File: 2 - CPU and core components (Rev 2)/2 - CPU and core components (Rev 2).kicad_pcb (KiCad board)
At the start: 2 copper layers, 152.3 x 106.7 mm, 76 parts, among them J1 READ INT MODE, J10 COM 3, J11 COM3 SWAP RX/TX, J2 BUS 1, J3 SIO1 CLK SRC, J4 COM 1, J5 COM 2, J6 SIO2 CLK SRC, J7 COM3 RX 232 BYPASS, J8 COM3 TTL OR 232, J9 DB9 VCC BYPASS, U1 ATF16V8B, U10 AS6C4008, U11 Z84C3010 CTC, U12 Z84C4010, U13 MCP2221A, U14 MCP2221A, U15 Z84C4010, U16 MAX232, U2 ATF22V10C, U3 ATF16V8B, U4 74HCT573, U5 74HCT32, U6 74HCT374, U7 74HCT244, U8 Z84C0010, U9 SST39SF010, X1 10 MHz, X2 3.6864 MHz

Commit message: Replacing a lot of TTL chips by 2 PLDs. Also, added blinkenlights.
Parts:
- removed the C19 at (168.0, 46.7)
- removed C20: 1µF, Capacitor_THT:C_Disc_D3.4mm_W2.1mm_P2.50mm
- removed C21, C22, C23, C24: 1uF, Capacitor_THT:C_Disc_D3.4mm_W2.1mm_P2.50mm
- removed D10, D9: RX3, LED_THT:LED_D3.0mm_Horizontal_O1.27mm_Z2.0mm_Clear
- removed the D7 at (109.3, 95.4)
- removed the D8 at (109.3, 85.3)
- removed J10: COM 3, Connector_Dsub:DSUB-9_Male_Horizontal_P2.77x2.84mm_EdgePinOffset4.94mm_Housed_MountingHolesOffset7.48mm
- removed J11: COM3 SWAP RX/TX, Connector_PinHeader_2.54mm:PinHeader_2x03_P2.54mm_Vertical
- removed J6: SIO2 CLK SRC, Connector_PinHeader_2.54mm:PinHeader_1x03_P2.54mm_Vertical
- removed J7: COM3 RX 232 BYPASS, Connector_PinHeader_2.54mm:PinHeader_1x02_P2.54mm_Vertical
- removed J8: COM3 TTL OR 232, Connector_PinHeader_2.54mm:PinHeader_2x03_P2.54mm_Vertical
- removed J9: DB9 VCC BYPASS, Connector_PinHeader_2.54mm:PinHeader_1x02_P2.54mm_Vertical
- removed R7: 3K3, Resistor_THT:R_Axial_DIN0207_L6.3mm_D2.5mm_P10.16mm_Horizontal
- removed R8: 330, Resistor_THT:R_Axial_DIN0207_L6.3mm_D2.5mm_P10.16mm_Horizontal
- removed R9: 220, Resistor_THT:R_Axial_DIN0207_L6.3mm_D2.5mm_P10.16mm_Horizontal
- removed the U15 at (171.2, 74.8)
- removed the U16 at (225.9, 37.8)
- removed the U3 at (161.2, 125.1)
- removed the U4 at (196.8, 110.9)
- added BAR1: F2010BW, 0_Library:BAR_GRAPH_8, F.Cu at (120.6, 125.2)
- added C10: 1µF, Capacitor_THT:C_Disc_D3.0mm_W2.0mm_P2.50mm, F.Cu at (52.0, 82.4)
- added RN5: 330, Resistor_THT:R_Array_SIP9, F.Cu at (109.2, 126.4)
- added U17: 74HCT240, Package_DIP:DIP-20_W7.62mm_Socket, F.Cu at (73.0, 53.4)
- added U2: 74HCT74, Package_DIP:DIP-14_W7.62mm_Socket, F.Cu at (18.1, 49.1)
- added U5: ATF22V10C, Package_DIP:DIP-24_W7.62mm, F.Cu at (41.2, 68.5)
- added U8: 74HCT32, Package_DIP:DIP-14_W7.62mm_Socket, F.Cu at (29.9, 49.1)
- added U9: 74HCT373, Package_DIP:DIP-20_W7.62mm_Socket, F.Cu at (29.9, 68.6)
- C1, C2, C3, C4, C7: footprint Capacitor_THT:C_Disc_D3.4mm_W2.1mm_P2.50mm -> Capacitor_THT:C_Disc_D3.0mm_W1.6mm_P2.50mm
- C5, C6, C8, C9: footprint Capacitor_THT:C_Disc_D3.4mm_W2.1mm_P2.50mm -> Capacitor_THT:C_Disc_D3.0mm_W2.0mm_P2.50mm
- U1: value ATF16V8B -> 74HCT132; footprint Package_DIP:DIP-20_W7.62mm_Socket -> Package_DIP:DIP-14_W7.62mm_Socket
- U6: value 74HCT374 -> 74HCT373
- U7: value 74HCT244 -> 74HCT273
- X1: value 10 MHz -> 20 MHz
- X2: value 3.6864 MHz -> 7.3728 MHz
- moved R6 187.1 mm to (294.6, 52.1)
- moved R4 187.0 mm to (291.3, 52.1)
- moved R5 187.0 mm to (291.2, 56.6)
- moved R3 187.0 mm to (297.6, 66.9)
- moved R1 183.5 mm to (295.9, 84.5)
- moved C5 183.2 mm to (52.0, 68.2), turned to 0 degrees
- moved R2 179.0 mm to (299.0, 89.0)
- moved U3 169.6 mm to (57.7, 89.0)
- moved U1 166.7 mm to (6.40, 49.1), turned to 0 degrees
- moved C2 162.5 mm to (41.1, 51.7), turned to 0 degrees
- moved C4 159.8 mm to (41.1, 58.0), turned to 0 degrees
- moved D4 149.0 mm to (247.6, 70.5), turned to 90 degrees
- moved J1 139.9 mm to (49.5, 112.8)
- moved RN1 139.9 mm to (52.0, 136.7)
- moved RN2 139.9 mm to (80.0, 122.5)
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- renumbered C10 to C11, C11 to C12, C12 to C13, C13 to C14, C14 to C15, C15 to C16, C16 to C17, C17 to C18, C18 to C19, D1 to D3, D2 to D4, D3 to D5, D4 to D6, D5 to D7, D6 to D8, U8 to U10, U9 to U11, U10 to U12, U11 to U13, U12 to U14, U13 to U15, U14 to U16, U5 to U3, U2 to U4
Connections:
- J1 pad 1: ~{MODE1OE} -> ~{MODE1}
- J1 pad 3: ~{MODE2OE} -> ~{MODE0/2}
- J2 pad 1: TX -> unconnected-(J2-A1-Pad1)
- J2 pad 10: RX -> unconnected-(J2-A10-Pad10)
- J2 pad 58: unconnected-(J2-B27-Pad58) -> CTCLK1
- J2 pad 59: unconnected-(J2-B28-Pad59) -> IE
- J2 pad 97: /USR8 -> ~{RAM_OE}
- RN4 pad 2: SIO1_IEI -> IE
- RN4 pad 3: SIO2_IEI -> CTC_IEI
- RN4 pad 4: CTC_IEI -> unconnected-(RN4-R3-Pad4)
- RN4 pad 5: STAT3A -> unconnected-(RN4-R4-Pad5)
- U1 pad 10: GND -> +5V
- U1 pad 11: RxD3 -> unconnected-(U1-Pad11)
- U1 pad 12: TxD3 -> +5V
- U1 pad 13: Rx3LED -> +5V
- U1 pad 14: Tx3LED -> +5V
- U1 pad 2: ~{MREQ} -> /Glue Logic/~{ROM_SEL}
- U1 pad 3: ~{RD} -> /Glue Logic/~{RAM_SEL}
- U1 pad 4: A15 -> /Glue Logic/~{RAM_SEL}
- U1 pad 5: BA19 -> ~{MODE1}
- U1 pad 6: BA20 -> /Glue Logic/~{ROM_SEL}
- U1 pad 7: BA21 -> GND
- U1 pad 8: BA22 -> unconnected-(U1-Pad8)
- U1 pad 9: ~{BANKRD} -> +5V
- U12 pad 22: ~{RAMCS1} -> ~{RAM_CS1}
- U14 pad 35: ~{SIO1_CS} -> ~{SIO_CS}
- U14 pad 6: SIO1_IEI -> IE
- U3 pad 1: A15 -> /Glue Logic/~{RAM_SEL}
- U3 pad 10: Net-(U6-O2) -> Net-(U7-Q2)
- U3 pad 13: Net-(U6-O3) -> Net-(U7-Q3)
- U3 pad 2: Net-(U6-O0) -> ~{RD}
- U3 pad 3: BA15 -> ~{RAM_OE}
- U3 pad 4: A15 -> ~{MREQ}
- U3 pad 5: Net-(U6-O1) -> /Glue Logic/~{ROM_SEL}
- U3 pad 6: BA16 -> ~{ROM_CS}
- U4 pad 20: Net-(U4-D4) -> Net-(U6-D4)
- U4 pad 21: Net-(U4-D3) -> Net-(U6-D3)
- U4 pad 22: Net-(U4-D2) -> Net-(U6-D2)
- U4 pad 23: Net-(U4-D1) -> Net-(U6-D1)
- U6 pad 1: GND -> Net-(J1-Pin_2)
- U6 pad 11: ~{BANKWR} -> ~{M1}
- U6 pad 12: BA19 -> D4
- U6 pad 13: D4 -> Net-(U6-D4)
- U6 pad 14: D5 -> GND
- U6 pad 15: BA20 -> D5
- U6 pad 16: BA21 -> D6
- U6 pad 17: D6 -> GND
- U6 pad 18: D7 -> GND
- U6 pad 19: BA22 -> D7
- U6 pad 2: Net-(U6-O0) -> D0
- U6 pad 3: D0 -> GND
- U6 pad 4: D1 -> Net-(U6-D1)
- U6 pad 5: Net-(U6-O1) -> D1
- U6 pad 6: Net-(U6-O2) -> D2
- U6 pad 7: D2 -> Net-(U6-D2)
- U6 pad 8: D3 -> Net-(U6-D3)
- U6 pad 9: Net-(U6-O3) -> D3
- U7 pad 1: ~{BANKRD} -> ~{RESET}
- U7 pad 11: BA22 -> ~{BANK_WR}
- U7 pad 12: D3 -> BA19
- U7 pad 13: BA21 -> D4
- U7 pad 14: D2 -> D5
- U7 pad 16: D1 -> BA21
- U7 pad 17: BA19 -> D6
- U7 pad 18: D0 -> D7
- U7 pad 19: ~{BANKRD} -> BA22
- U7 pad 2: BA15 -> Net-(U7-Q0)
- U7 pad 3: D4 -> D0
- U7 pad 4: BA16 -> D1
- U7 pad 5: D5 -> Net-(U7-Q1)
- U7 pad 6: BA17 -> Net-(U7-Q2)
- U7 pad 7: D6 -> D2
- U7 pad 8: BA18 -> D3
- U7 pad 9: D7 -> Net-(U7-Q3)
- X1 pad 5: CLK -> Net-(U2A-C)
- X2 pad 5: CLK2 -> Net-(U2B-C)
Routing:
- net +5V: track 177.9 -> 0.00 mm, vias 4 -> 0
- added copper zone on In2.Cu, net +5V
- added copper zone on In1.Cu, net GND
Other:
- copper layers 2 -> 4

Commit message: Added Interrupt Enable daisy chain jumpers between the ISA slots
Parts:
- moved U17 204.7 mm to (274.9, 19.7), turned to 90 degrees
- moved RN5 195.4 mm to (283.8, 38.8), turned to 0 degrees
- moved RN1 185.5 mm to (180.3, 2.72)
- moved RN2 185.5 mm to (208.2, -11.5)
- moved U4 185.5 mm to (180.3, -0.57)
- moved J3 183.6 mm to (167.6, -102.8)
- moved BAR1 180.7 mm to (285.1, 50.2), turned to 90 degrees
- moved D8 143.6 mm to (247.6, 47.1), turned to 90 degrees
- moved D7 141.4 mm to (247.6, 67.4), turned to 90 degrees
- moved D6 141.2 mm to (247.6, 52.2), turned to 90 degrees
- moved D5 139.7 mm to (247.6, 72.4), turned to 90 degrees
- moved C1 125.4 mm to (32.9, -76.6)
- moved C10 125.4 mm to (43.7, -42.7)
- moved C11 125.4 mm to (159.8, -56.6)
- moved C12 125.4 mm to (101.4, -80.9)
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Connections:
- J1 pad 3: ~{MODE0/2} -> /Glue Logic/~{MODE0/2}
- U5 pad 18: ~{MODE0/2} -> unconnected-(U5-I/O-Pad18)
- U8 pad 11: unconnected-(U8-Pad11) -> /Glue Logic/~{MODE0/2}
- U8 pad 12: +5V -> ~{IORQ}
- U8 pad 13: +5V -> ~{M1}

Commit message: Finished component placement, currently routing.
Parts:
- added C20: 1µF, Capacitor_THT:C_Disc_D3.0mm_W2.0mm_P2.50mm, F.Cu at (213.3, 104.2)
- added C21: 1µF, Capacitor_THT:C_Disc_D3.0mm_W2.0mm_P2.50mm, F.Cu at (213.3, 119.4)
- added D1: DTRA, LED_THT:LED_D3.0mm_Horizontal_O1.27mm_Z2.0mm_Clear, F.Cu at (239.3, 40.1)
- added D2: DTRB, LED_THT:LED_D3.0mm_Horizontal_O1.27mm_Z2.0mm_Clear, F.Cu at (244.4, 40.1)
- C10: footprint Capacitor_THT:C_Disc_D3.0mm_W2.0mm_P2.50mm -> Capacitor_THT:C_Disc_D3.4mm_W2.1mm_P2.50mm
- J1: value READ INT MODE -> INT MODE
- U5: footprint Package_DIP:DIP-24_W7.62mm -> Package_DIP:DIP-24_W7.62mm_Socket
- moved U9 238.7 mm to (208.9, 91.5), turned to 90 degrees
- moved U8 231.1 mm to (163.1, 106.7), turned to 90 degrees
- moved U2 222.3 mm to (136.5, 106.7), turned to 90 degrees
- moved U1 220.2 mm to (155.5, 91.5), turned to 90 degrees
- moved U6 210.1 mm to (178.4, 91.5), turned to 90 degrees
- moved C15 195.9 mm to (177.7, 116.9), turned to -90 degrees
- moved C4 194.7 mm to (96.5, 116.9), turned to -90 degrees
- moved J3 192.3 mm to (236.2, 76.9), turned to 180 degrees
- moved U7 192.0 mm to (180.9, 122.0), turned to 90 degrees
- moved C12 191.8 mm to (160.0, 101.7)
- moved J1 189.8 mm to (211.4, 71.8)
- moved C9 188.0 mm to (137.1, 116.9), turned to -90 degrees
- moved C7 181.0 mm to (141.6, 80.7)
- moved C8 175.9 mm to (133.3, 101.7), turned to -90 degrees
- moved C3 170.4 mm to (90.1, 90.3), turned to -90 degrees
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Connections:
- net Net-(J4-D+) renamed /SIO/D1+
- net Net-(J4-D-) renamed /SIO/D1-
- net Net-(J5-D+) renamed /SIO/D2+
- net Net-(J5-D-) renamed /SIO/D2-
- D3 pad 2: +5V -> Net-(D3-A)
- D4 pad 2: +5V -> Net-(D4-A)
- D5 pad 2: +5V -> Net-(D5-A)
- D6 pad 2: +5V -> Net-(D6-A)
- D7 pad 2: +5V -> Net-(D7-A)
- D8 pad 2: +5V -> Net-(D8-A)
- J2 pad 1: unconnected-(J2-A1-Pad1) -> /TX
- J2 pad 10: unconnected-(J2-A10-Pad10) -> /RX
- J2 pad 58: CTCLK1 -> CTCLK0
- J3 pad 3: CTCLK0 -> CTCLK1
- R1 pad 1: Net-(U15-GP2_(USB)) -> Net-(D3-A)
- R1 pad 2: Net-(D3-K) -> +5V
- R2 pad 1: Net-(U16-GP2_(USB)) -> Net-(D4-A)
- R2 pad 2: Net-(D4-K) -> +5V
- R3 pad 1: Net-(U15-GP1_(Tx)) -> Net-(D5-A)
- R3 pad 2: Net-(D5-K) -> +5V
- R4 pad 1: Net-(U16-GP1_(Tx)) -> Net-(D6-A)
- R4 pad 2: Net-(D6-K) -> +5V
- R5 pad 1: Net-(U15-GP0_(Rx)) -> Net-(D7-A)
- R5 pad 2: Net-(D7-K) -> +5V
- R6 pad 1: Net-(U16-GP0_(Rx)) -> Net-(D8-A)
- R6 pad 2: Net-(D8-K) -> +5V
- RN2 pad 2: ~{IRQ}8 -> ~{IRQ}11
- RN2 pad 3: ~{IRQ}9 -> ~{IRQ}12
- RN2 pad 5: ~{IRQ}11 -> ~{IRQ}13
- RN2 pad 6: ~{IRQ}12 -> ~{IRQ}9
- RN2 pad 7: ~{IRQ}13 -> ~{IRQ}14
- RN2 pad 8: ~{IRQ}14 -> ~{IRQ}8
- RN4 pad 2: IE -> ~{NMI}
- RN4 pad 3: CTC_IEI -> ~{INT}
- RN4 pad 4: unconnected-(RN4-R3-Pad4) -> ~{WAIT}
- RN4 pad 5: unconnected-(RN4-R4-Pad5) -> ~{BUSRQ}
- RN4 pad 6: ~{NMI} -> IE
- RN4 pad 7: ~{WAIT} -> CTC_IEI
- RN4 pad 8: ~{INT} -> R_FTRB
- RN4 pad 9: ~{BUSRQ} -> R_FTRA
- U1 pad 10: +5V -> Net-(U14-~{DTRA})
- U1 pad 11: unconnected-(U1-Pad11) -> Net-(D2-K)
- U1 pad 12: +5V -> Net-(U14-~{DTRB})
- U1 pad 13: +5V -> Net-(U14-~{DTRB})
- U1 pad 8: unconnected-(U1-Pad8) -> Net-(D1-K)
- U1 pad 9: +5V -> Net-(U14-~{DTRA})
- U12 pad 22: ~{RAM_CS1} -> ~{RAM_CS}
- U14 pad 16: unconnected-(U14-~{DTRA}-Pad16) -> Net-(U14-~{DTRA})
- U14 pad 25: unconnected-(U14-~{DTRB}-Pad25) -> Net-(U14-~{DTRB})
- U15 pad 2: Net-(U15-GP0_(Rx)) -> Net-(D7-K)
- U15 pad 3: Net-(U15-GP1_(Tx)) -> Net-(D5-K)
- U15 pad 7: Net-(U15-GP2_(USB)) -> Net-(D3-K)
- U16 pad 2: Net-(U16-GP0_(Rx)) -> Net-(D8-K)
- U16 pad 3: Net-(U16-GP1_(Tx)) -> Net-(D6-K)
- U16 pad 7: Net-(U16-GP2_(USB)) -> Net-(D4-K)
- U5 pad 10: A4 -> A7
- U5 pad 11: A3 -> A15
- U5 pad 17: ~{RAM_CS1} -> unconnected-(U5-I/O-Pad17)
- U5 pad 18: unconnected-(U5-I/O-Pad18) -> ~{RAM_CS}
- U5 pad 6: A15 -> A3
- U5 pad 7: A7 -> A4
- U5 pad 8: A6 -> A5
- U5 pad 9: A5 -> A6
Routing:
- net +5V: track 0.00 -> 179.6 mm, vias 0 -> 3
- net /SIO/D2+: track 0.00 -> 25.4 mm
- net /SIO/D1+: track 0.00 -> 24.0 mm
- net /SIO/D2-: track 0.00 -> 22.4 mm
- net ~{NMI}: track 0.00 -> 21.2 mm
- net ~{INT}: track 0.00 -> 21.2 mm
- net ~{IRQ}8: track 0.00 -> 18.9 mm
- net /SIO/D1-: track 0.00 -> 18.4 mm
- net ~{IRQ}9: track 0.00 -> 16.3 mm
- net ~{IRQ}15: track 0.00 -> 14.0 mm
- net ~{IRQ}10: track 0.00 -> 13.7 mm
- net ~{IRQ}14: track 0.00 -> 9.30 mm
- net ~{IRQ}13: track 0.00 -> 6.95 mm
- net ~{IRQ}7: track 0.00 -> 4.98 mm
- net ~{IRQ}5: track 0.00 -> 4.98 mm
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- removed copper zone on In2.Cu, net +5V
- removed copper zone on In1.Cu, net GND
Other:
- board size 152.3 x 106.7 mm -> 167 x 106.7 mm
- copper layers 4 -> 2

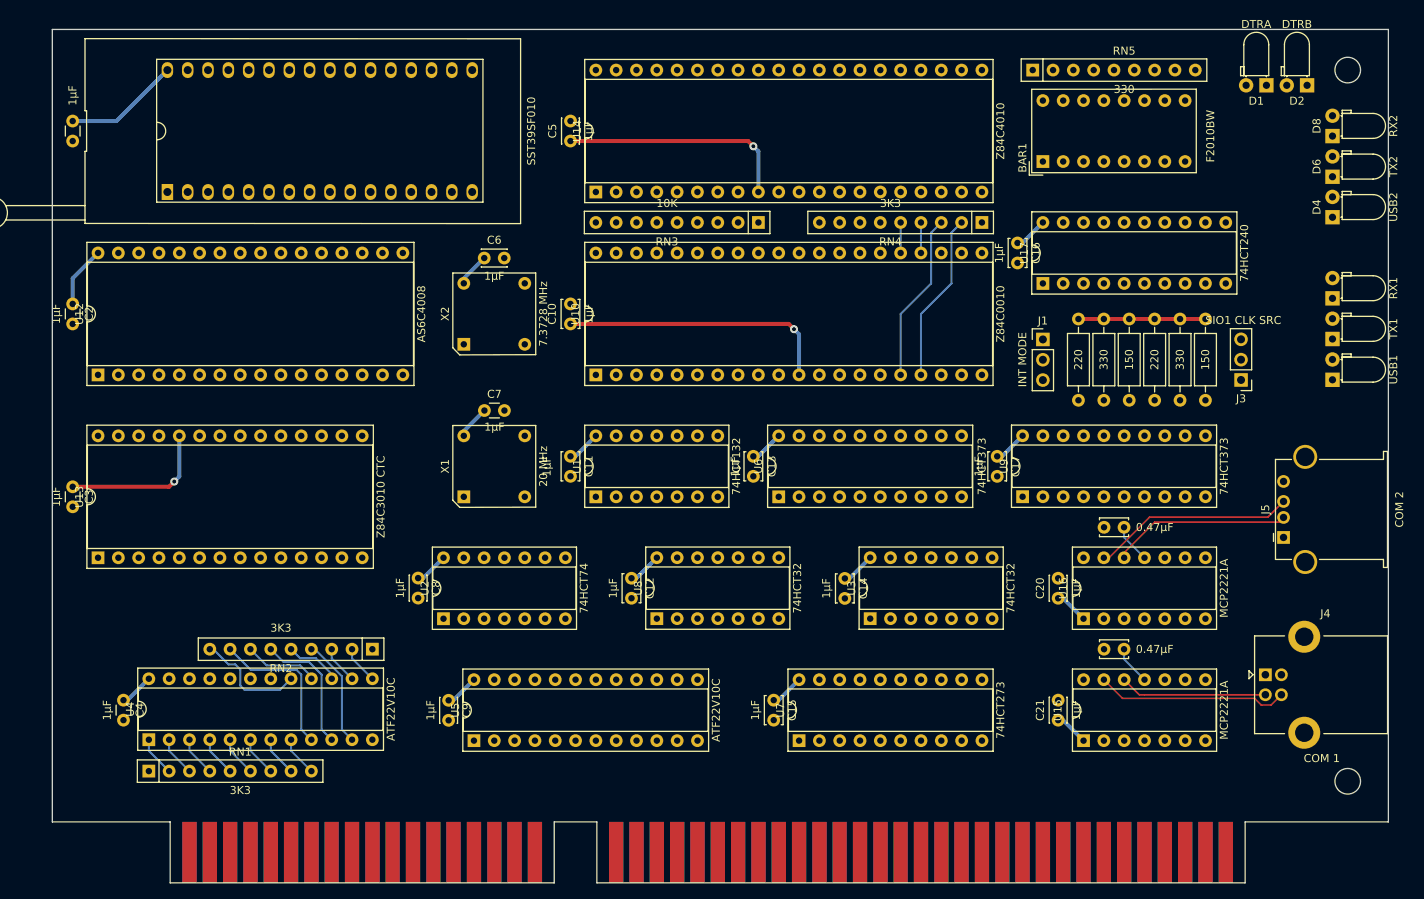
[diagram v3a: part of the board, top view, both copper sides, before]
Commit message: Adding buffers to the CPU card
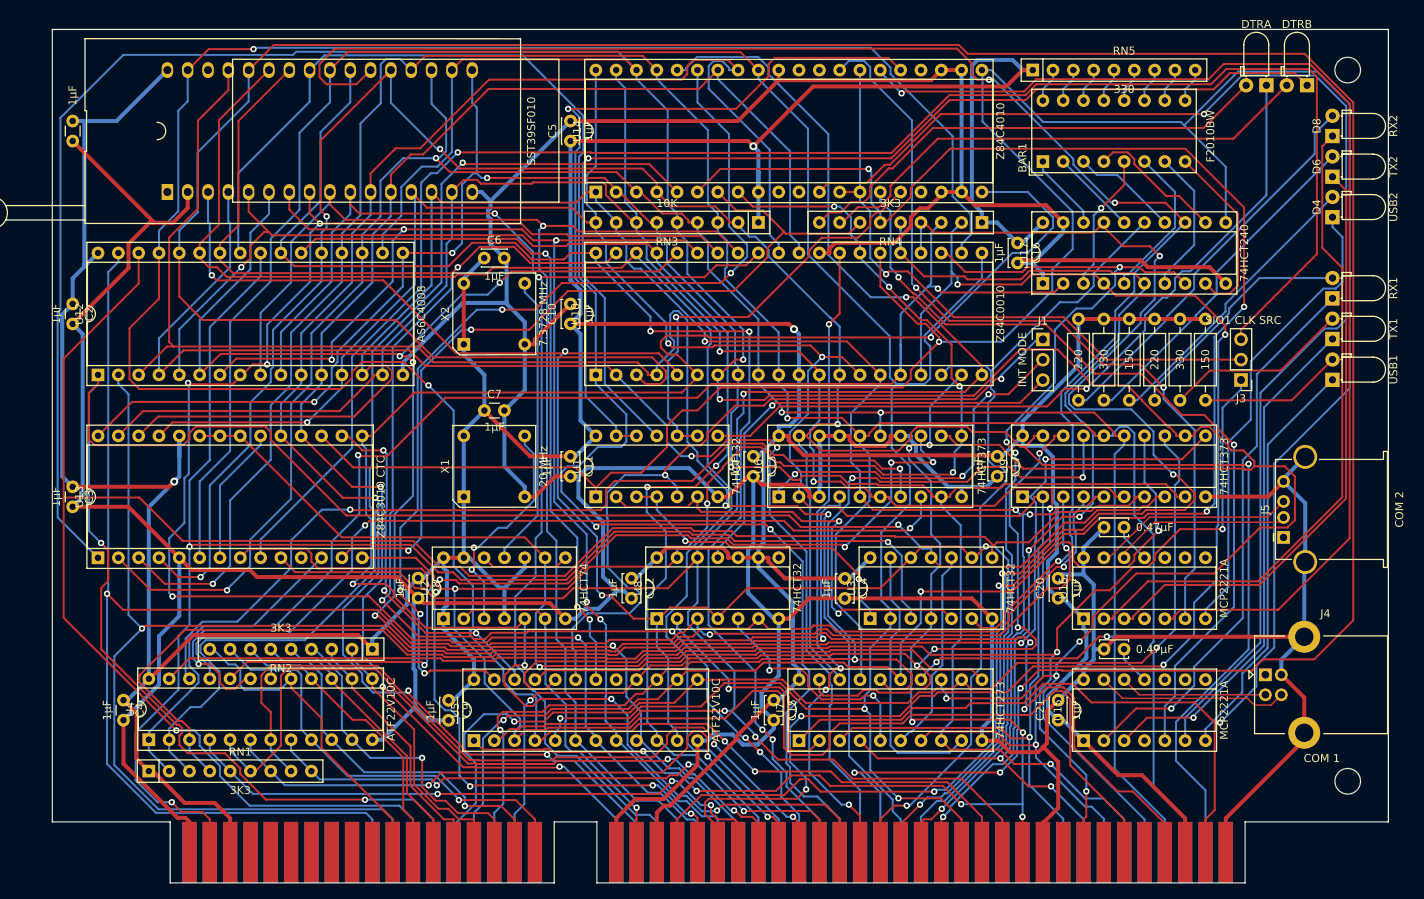
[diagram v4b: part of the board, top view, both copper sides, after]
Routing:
- net GND: track 0.00 -> 798.2 mm
- net +5V: track 179.6 -> 721.3 mm
- net D4: track 0.00 -> 448.8 mm, vias 0 -> 5
- net A13: track 0.00 -> 395.7 mm, vias 0 -> 3
- net ~{RESET}: track 0.00 -> 381.5 mm, vias 0 -> 2
- net D7: track 0.00 -> 320.3 mm, vias 0 -> 5
- net ~{WR}: track 0.00 -> 317.9 mm, vias 0 -> 4
- net ~{RD}: track 0.00 -> 308.4 mm, vias 0 -> 3
- net D6: track 0.00 -> 308.0 mm, vias 0 -> 2
- net D5: track 0.00 -> 288.2 mm, vias 0 -> 6
- net ~{IORQ}: track 0.00 -> 272.5 mm, vias 0 -> 4
- net ~{M1}: track 0.00 -> 271.1 mm, vias 0 -> 6
- net D0: track 0.00 -> 267.7 mm, vias 0 -> 4
- net D3: track 0.00 -> 267.3 mm, vias 0 -> 5
- net D2: track 0.00 -> 266.1 mm, vias 0 -> 4
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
